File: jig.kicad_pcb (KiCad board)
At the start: 4 copper layers, 139.5 x 136.2 mm, 18 parts, among them J1 ServoAnalog, J12 ROMI-Encoder, J13 ROMI-Encoder, J14 THING, J15 THING, J2 Conn_01x19_Female, J3 LineSensor, J4 LineSensor, J5 THING, J6 Conn_02x19_Odd_Even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

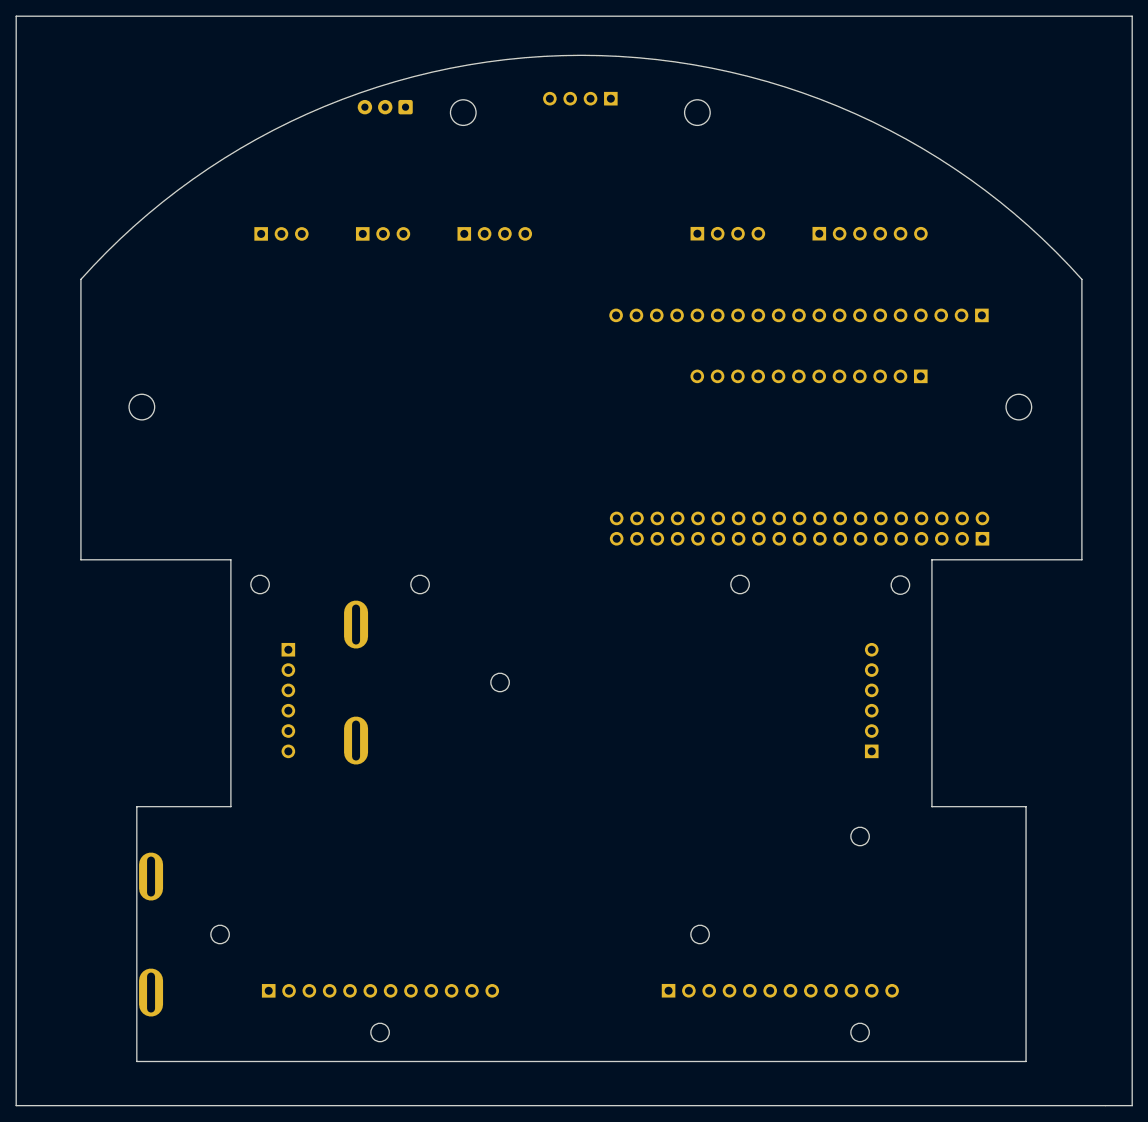
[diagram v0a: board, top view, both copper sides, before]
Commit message: Added jig PCB
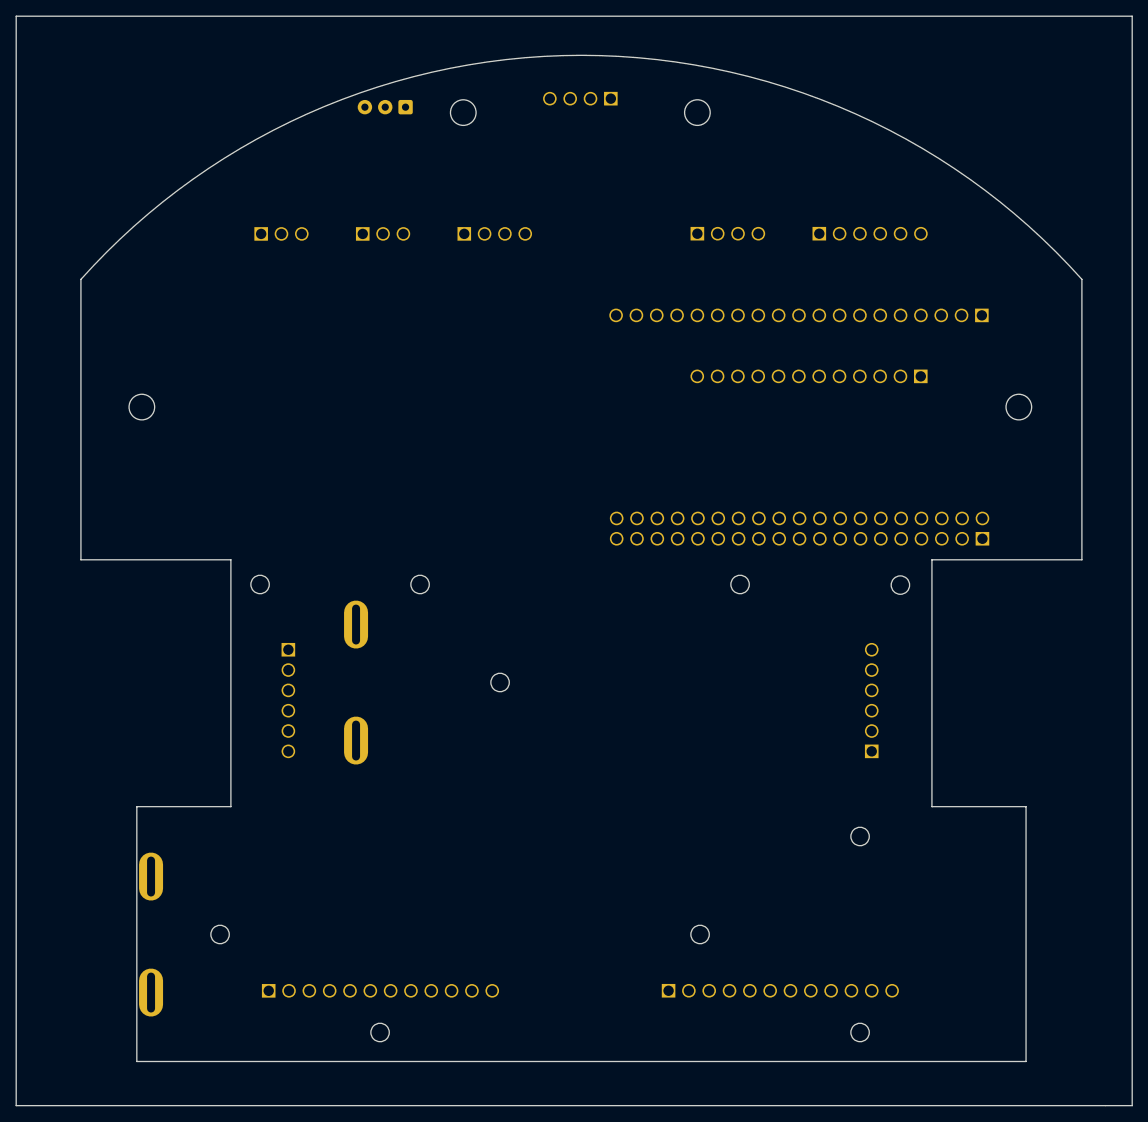
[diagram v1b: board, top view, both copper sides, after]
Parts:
- J1, J7, J9: footprint Connector_PinSocket_2.54mm:PinSocket_1x04_P2.54mm_Vertical -> jig:PinSocket_1x04_P2.54mm_Vertical
- J12, J13, J8: footprint Connector_PinSocket_2.54mm:PinSocket_1x06_P2.54mm_Vertical -> jig:PinSocket_1x06_P2.54mm_Vertical_1_3mm
- J14, J15, J5: footprint Connector_PinSocket_2.54mm:PinSocket_1x12_P2.54mm_Vertical -> jig:PinSocket_1x12_P2.54mm_Vertical_1_3mm
- J2: footprint Connector_PinSocket_2.54mm:PinSocket_1x19_P2.54mm_Vertical -> jig:PinSocket_1x19_P2.54mm_Vertical
- J3, J4: footprint Connector_PinSocket_2.54mm:PinSocket_1x03_P2.54mm_Vertical -> jig:PinSocket_1x03_P2.54mm_Vertical
- J6: footprint Connector_PinSocket_2.54mm:PinSocket_2x19_P2.54mm_Vertical -> jig:PinSocket_2x19_P2.54mm_Vertical
